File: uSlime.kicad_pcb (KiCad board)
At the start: 2 copper layers, 25 x 22.6 mm, 36 parts, among them CN1 X1502WR-05K-N0SN, CN2 1.25T-2AW, J1 USB_C_Receptacle_USB2.0_14P, U1 ESP32-C6-MINI-1, U3 AP2112K-3.3TRG1, U4 MCP73831T-2ACI/OT, U5 BNO085, U6 MSK-12C02_SMD_SPDT_SWITCH

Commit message: Add NC points
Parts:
- added TP7: VBUS, TestPoint:TestPoint_Pad_2.0x2.0mm, B.Cu at (106.2, 108.1)
- moved G*** 1.39 mm to (115.0, 100.1)
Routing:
- net VBUS: track 31.6 -> 34.7 mm
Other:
- board text added: "+3.3V"
- board text added: "CHRG"
- board text added: "Created by:"
- board text added: "GND"
- board text added: "IO20"
- board text added: "IO21"
- board text added: "RST"
- board text added: "SCL"
- board text added: "SDA"
- board text added: "STAT"
- board text added: "VIN +5V"
- board text added: "pei-lu"

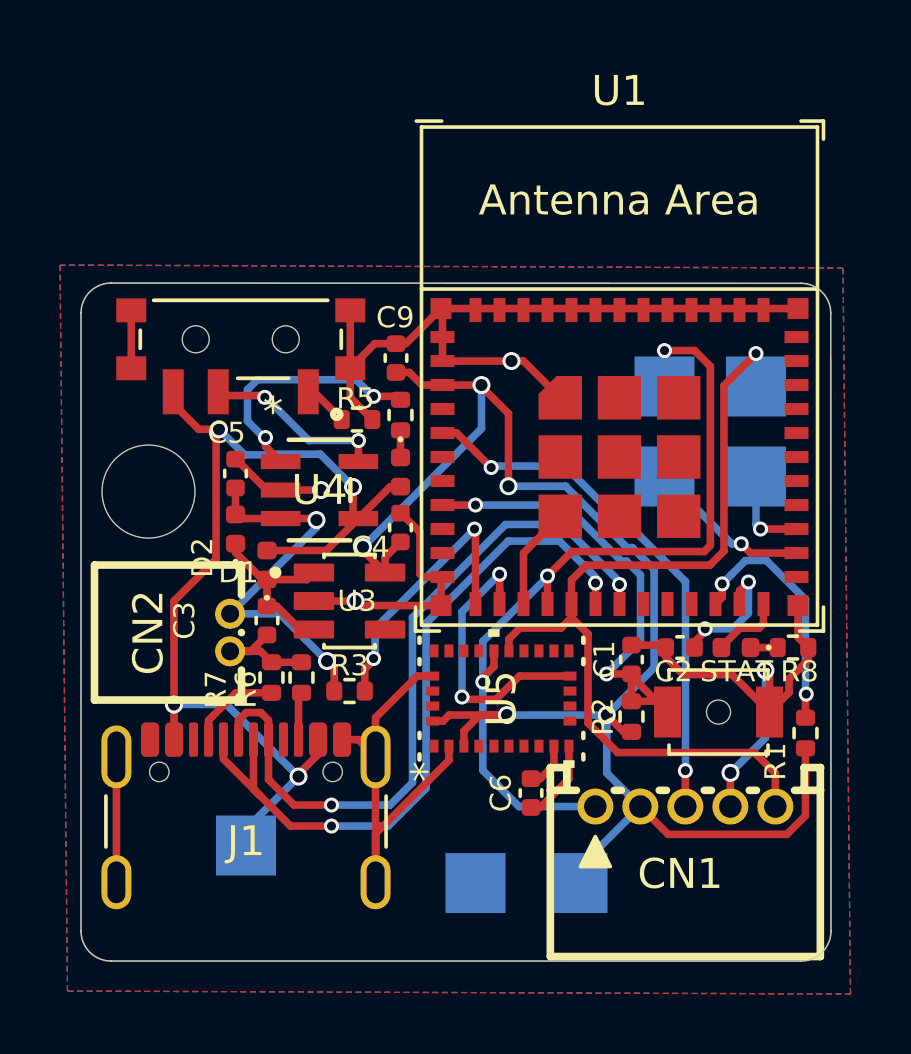
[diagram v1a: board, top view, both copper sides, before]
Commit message: Revamp pwr resistor, cap placement, fix switch sym
Fix placement of resistors and capacitor placement b/c additional
components were added to power circuit and weren't correct...

Also fixed switch symbol so wires actually connect to it in schematic
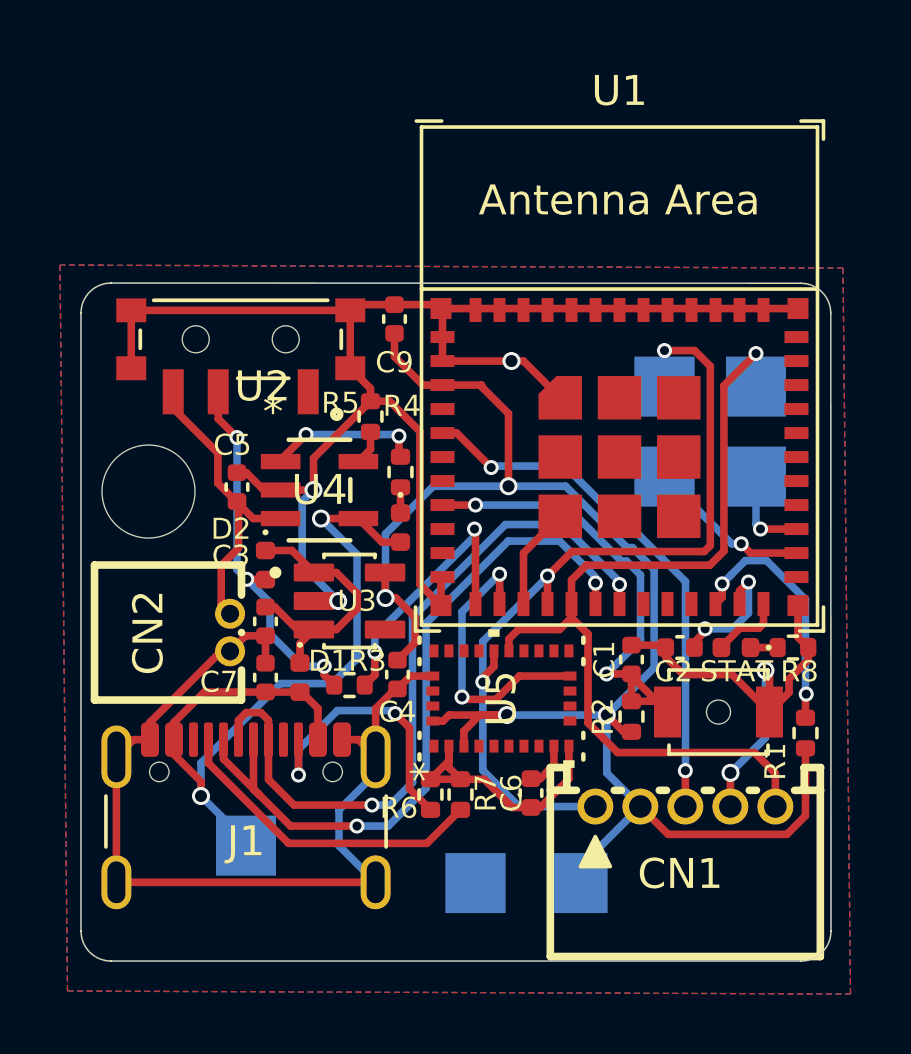
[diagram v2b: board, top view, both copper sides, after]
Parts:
- added C7: 10μF, Capacitor_SMD:C_0402_1005Metric, F.Cu at (106.8, 102.5)
- C5: value 10uF -> 10μF
- C6, C9: value 0.1 uF -> 0.1uF
- R5: value 4.7k -> 2k
- moved R7 7.41 mm to (113.3, 106.4)
- moved R6 5.81 mm to (112.3, 106.4)
- moved C4 4.90 mm to (111.2, 102.4), turned to -90 degrees
- moved D1 3.91 mm to (108.0, 102.5), turned to -90 degrees
- moved R4 1.90 mm to (111.3, 95.7)
- moved CHRG1 1.85 mm to (111.3, 97.5)
- moved D2 1.56 mm to (106.8, 98.8), turned to -90 degrees
- moved C9 1.30 mm to (111.1, 90.5)
- moved R5 0.46 mm to (110.3, 93.8), turned to 90 degrees
- moved C5 0.45 mm to (105.8, 96.2), turned to 90 degrees
- moved R3 0.20 mm to (109.6, 102.8)
- moved C3 0.06 mm to (106.8, 100.6)
- renumbered U6 to U2
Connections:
- C5 pad 1: GND -> VBAT
- C5 pad 2: VBAT -> GND
- D2 pad 2: VBAT -> Net-(D2-A)
- R3 pad 1: VBAT -> Net-(D2-A)
- R5 pad 1: GND -> Net-(U4-PROG)
- R5 pad 2: Net-(R5-Pad2) -> GND
- U2 pad COM: Net-(U4-PROG) -> Net-(D2-A)
- U2 pad L1: VBUS -> VBAT
- U2 pad L2: Net-(R5-Pad2) -> unconnected-(U2-PadL2)
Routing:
- net GND: track 85.1 -> 114.9 mm
- net Net-(D2-A): track 0.00 -> 12.4 mm, vias 0 -> 3
- net Net-(J1-CC2): track 1.60 -> 9.53 mm, vias 0 -> 2
- net Net-(J1-CC1): track 3.12 -> 10.8 mm
- net VBUS: track 34.7 -> 27.5 mm, vias 4 -> 2
- net Net-(U4-PROG): track 6.12 -> 1.16 mm, vias 2 -> 0
- net Net-(D1-K): track 6.06 -> 9.55 mm
- net Net-(U4-STAT): track 8.44 -> 5.08 mm
- net VBAT: track 13.0 -> 10.4 mm, vias 2 -> 0
- net +3.3V: track 52.2 -> 54.4 mm, vias 5 -> 4
- net Net-(R5-Pad2): track 1.50 -> 0.00 mm
